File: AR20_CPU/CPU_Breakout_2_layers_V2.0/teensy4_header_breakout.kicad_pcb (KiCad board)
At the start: 2 copper layers, 65 x 80 mm, 69 parts, among them SW1 SW_Push, SW2 SW_Push, T4 BreakoutBoardTeensy_Teensy_pi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, U1 S8211-46R

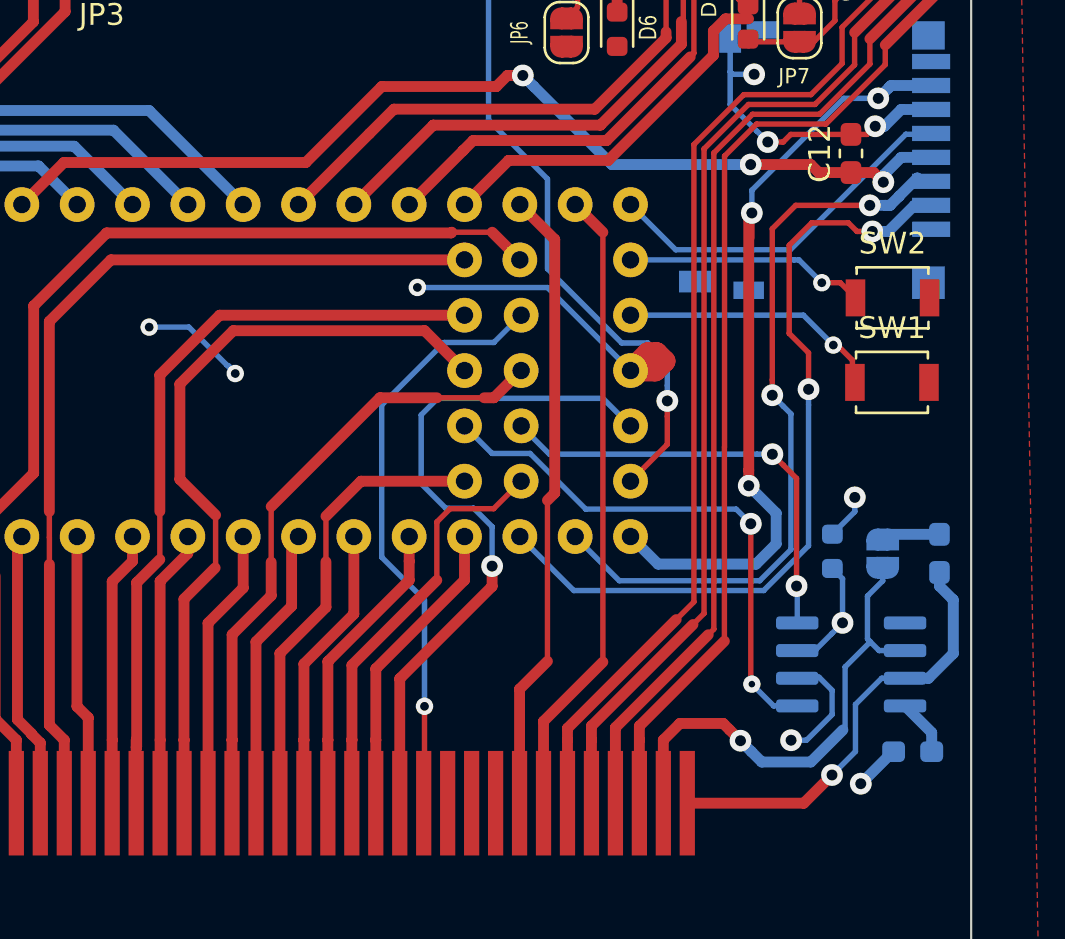
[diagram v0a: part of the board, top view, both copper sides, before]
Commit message: Endret SCLK pin til SD
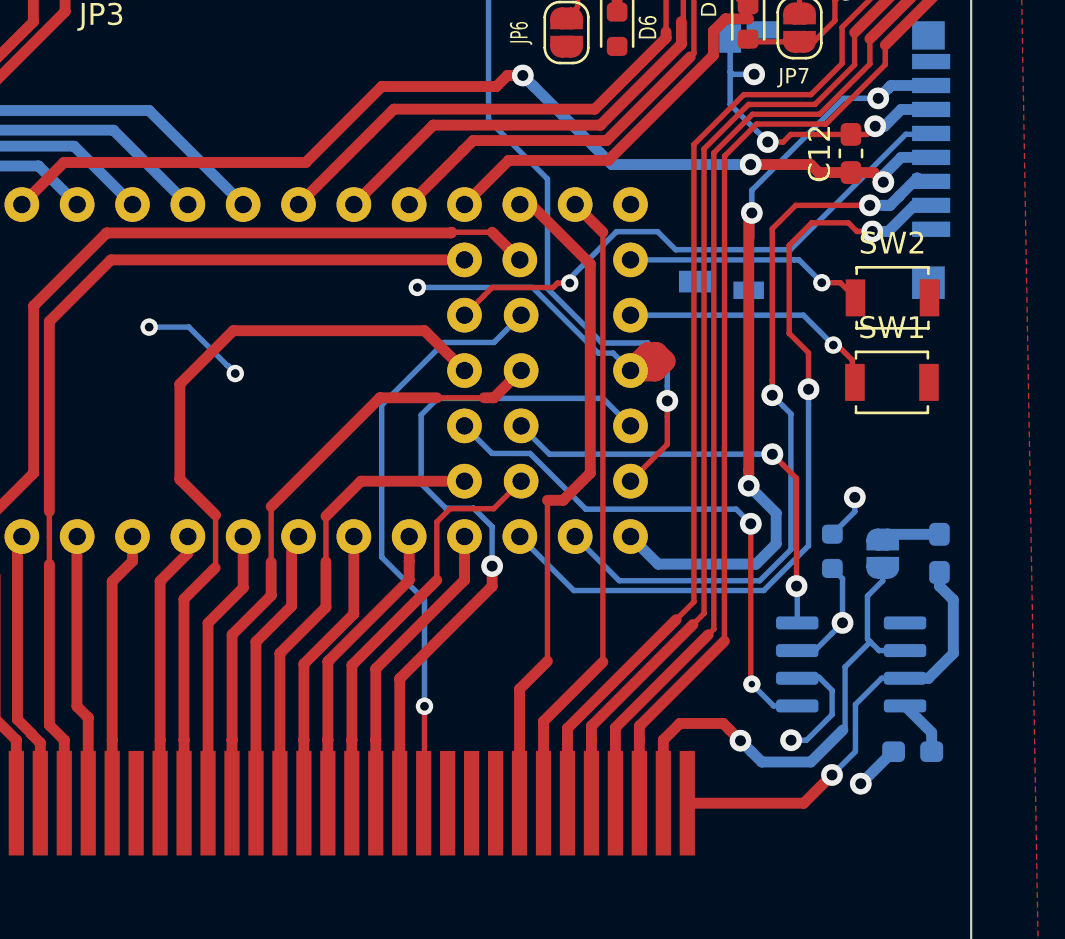
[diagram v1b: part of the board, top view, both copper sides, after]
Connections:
- MX1 pad 13: 27_A13 -> Ground
- SDcard1 pad 5: SCLK -> 27_A13
- T4 pad 28: SCLK -> (no net)
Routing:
- net SCLK: track 16.9 -> 0.00 mm
- net 27_A13: track 35.6 -> 25.7 mm, vias 0 -> 1
- net 21_RX3: track 28.8 -> 30.9 mm
- net VBAT: track 62.7 -> 63.2 mm
